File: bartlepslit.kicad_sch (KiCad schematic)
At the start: 91 parts, among them J1 Conn_01x06, J5 Conn_01x06, K1 SW_Push, K10 SW_Push, K11 SW_Push, K12 SW_Push, K13 SW_Push, K14 SW_Push, K15 SW_Push, K16 SW_Push, K17 SW_Push, K18 SW_Push, K19 SW_Push, K2 SW_Push, K20 SW_Push, K21 SW_Push, K22 SW_Push, K23 SW_Push, K24 SW_Push, K25 SW_Push, K26 SW_Push, K27 SW_Push, K28 SW_Push, K29 SW_Push, K3 SW_Push, K30 SW_Push, K31 SW_Push, K32 SW_Push, K33 SW_Push, K34 SW_Push, K35 SW_Push, K36 SW_Push, K37 SW_Push, K38 SW_Push, K39 SW_Push, K4 SW_Push, K40 SW_Push, K41 SW_Push, K42 SW_Push, K5 SW_Push, K6 SW_Push, K7 SW_Push, K8 SW_Push, K9 SW_Push, U1 ProMicro

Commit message: feat: fixed orientation of diodes
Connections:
- net ROW_1: now also D19.2 (A), D22.1 (K), D25.2 (A), D28.1 (K), D31.2 (A), D34.1 (K); no longer D19.1 (K), D22.2 (A), D25.1 (K), D28.2 (A), D31.1 (K), D34.2 (A)
- net ROW_2: now also D20.2 (A), D23.1 (K), D26.2 (A), D29.1 (K), D32.2 (A), D35.1 (K); no longer D20.1 (K), D23.2 (A), D26.1 (K), D29.2 (A), D32.1 (K), D35.2 (A)
- net ROW_3: now also D21.2 (A), D24.1 (K), D27.2 (A), D30.1 (K), D33.2 (A), D36.1 (K); no longer D21.1 (K), D24.2 (A), D27.1 (K), D30.2 (A), D33.1 (K), D36.2 (A)
- net at K22.2: now also D22.2 (A); no longer D22.1 (K)
- net at K27.2: now also D27.1 (K); no longer D27.2 (A)
- net at K34.2: now also D34.2 (A); no longer D34.1 (K)
- net at K21.2: now also D21.1 (K); no longer D21.2 (A)
- net at K24.2: now also D24.2 (A); no longer D24.1 (K)
- net at K28.2: now also D28.2 (A); no longer D28.1 (K)
- net at K32.2: now also D32.1 (K); no longer D32.2 (A)
- net at K36.2: now also D36.2 (A); no longer D36.1 (K)
- net at K29.2: now also D29.2 (A); no longer D29.1 (K)
- net at K30.2: now also D30.2 (A); no longer D30.1 (K)
- net at K35.2: now also D35.2 (A); no longer D35.1 (K)
- net at K26.2: now also D26.1 (K); no longer D26.2 (A)
- net at K31.2: now also D31.1 (K); no longer D31.2 (A)
- net at K20.2: now also D20.1 (K); no longer D20.2 (A)
- net at K33.2: now also D33.1 (K); no longer D33.2 (A)
- net at K19.2: now also D19.1 (K); no longer D19.2 (A)
- net at K23.2: now also D23.2 (A); no longer D23.1 (K)
- net at K25.2: now also D25.1 (K); no longer D25.2 (A)
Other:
- moved on the sheet: D1, D10, D11, D12, D13, D14, D15, D16, D17, D18, D19, D2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

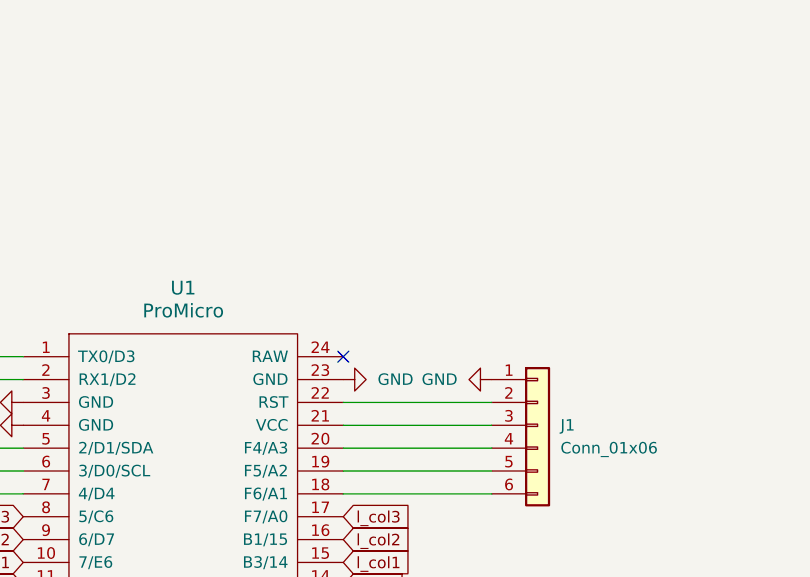
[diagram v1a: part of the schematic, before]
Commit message: feat: added missing reset switch
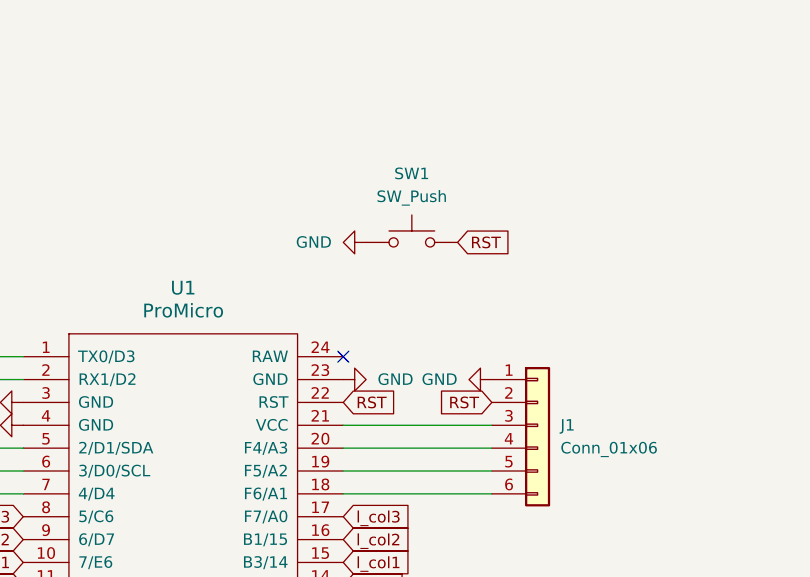
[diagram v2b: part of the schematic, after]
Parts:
- added SW1: SW_Push, Button_Switch_SMD:SW_Tactile_SPST_NO_Straight_CK_PTS636Sx25SMTRLFS, symbol Switch:SW_Push
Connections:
- net GND: now also SW1.1
- net RST: now reaches J1.2 (Pin_2), U1.22 (RST)
- net RST: now also SW1.2
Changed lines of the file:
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@@
-    (stroke (width 0) (type default))
-  )
-  (wire (pts (xy 91.44 106.68) (xy 107.95 106.68))
     (stroke (width 0) (type default))
   )
@@
     )
   )
+  (global_label "RST" (shape input) (at 91.44 106.68 0) (fields_autoplaced)
+    (effects (font (size 1.27 1.27)) (justify left))
+    (property "Intersheetrefs" "${INTERSHEET_REFS}" (at 97.8723 106.68 0)
+      (effects (font (size 1.27 1.27)) (justify left) hide)
+    )
+  )
   (global_label "L_ROW_4" (shape input) (at 227.33 114.3 0) (fields_autoplaced)
     (effects (font (size 1.27 1.27)) (justify left))
@@
     )
   )
+  (global_label "RST" (shape input) (at 107.95 106.68 180) (fields_autoplaced)
+    (effects (font (size 1.27 1.27)) (justify right))
+    (property "Intersheetrefs" "${INTERSHEET_REFS}" (at 101.5177 106.68 0)
+      (effects (font (size 1.27 1.27)) (justify right) hide)
+    )
+  )
   (global_label "L_ROW_2" (shape input) (at 257.81 40.64 0) (fields_autoplaced)
     (effects (font (size 1.27 1.27)) (justify left))
@@
     (effects (font (size 1.27 1.27)) (justify left))
     (property "Intersheetrefs" "${INTERSHEET_REFS}" (at 357.1942 54.61 0)
+      (effects (font (size 1.27 1.27)) (justify left) hide)
+    )
+  )
+  (global_label "RST" (shape input) (at 104.14 88.9 0) (fields_autoplaced)
+    (effects (font (size 1.27 1.27)) (justify left))
+    (property "Intersheetrefs" "${INTERSHEET_REFS}" (at 110.5723 88.9 0)
       (effects (font (size 1.27 1.27)) (justify left) hide)
     )
@@
     )
   )
+  (symbol (lib_id "Switch:SW_Push") (at 99.06 88.9 0) (unit 1)
+    (in_bom yes) (on_board yes) (dnp no) (fields_autoplaced)
+    (property "Reference" "SW1" (at 99.06 81.28 0)
+      (effects (font (size 1.27 1.27)))
+    )
+    (property "Value" "SW_Push" (at 99.06 83.82 0)
+      (effects (font (size 1.27 1.27)))
+    )
+    (property "Footprint" "Button_Switch_SMD:SW_Tactile_SPST_NO_Straight_CK_PTS636Sx25SMTRLFS" (at 99.06 83.82 0)
+      (effects (font (size 1.27 1.27)) hide)
+    )
+    (property "Datasheet" "~" (at 99.06 83.82 0)
+      (effects (font (size 1.27 1.27)) hide)
+    )
+    (pin "1")
+    (pin "2")
+    (instances
+      (project "bartlepslit"
+        (path "/9203b006-47ac-4f34-8cc4-2b709e3df56f"
+          (reference "SW1") (unit 1)
+        )
+      )
+    )
+  )
   (symbol (lib_id "Switch:SW_Push") (at 495.3 40.64 0) (unit 1)
     (in_bom yes) (on_board yes) (dnp no)
@@
         )
       )
+    )
+  )
+  (symbol (lib_id "power:GND") (at 93.98 88.9 270) (unit 1)
+    (in_bom yes) (on_board yes) (dnp no)
+    (property "Reference" "#PWR06" (at 87.63 88.9 0)
+      (effects (font (size 1.27 1.27)) hide)
+    )
+    (property "Value" "GND" (at 90.17 88.9 90)
+      (effects (font (size 1.27 1.27)) (justify right))
+    )
+    (property "Footprint" "" (at 93.98 88.9 0)
+      (effects (font (size 1.27 1.27)) hide)
+    )
+    (property "Datasheet" "" (at 93.98 88.9 0)
+      (effects (font (size 1.27 1.27)) hide)
+    )
+    (pin "1")
+    (instances
+      (project "japanese-connection"
+        (path "/91e0fa32-4625-43d1-992c-ecd8bd5a1db3"
+          (reference "#PWR06") (unit 1)
+        )
+      )
+      (project "bartlepslit"
+        (path "/9203b006-47ac-4f34-8cc4-2b709e3df56f"
+          (reference "#PWR06") (unit 1)
+        )
+      )
